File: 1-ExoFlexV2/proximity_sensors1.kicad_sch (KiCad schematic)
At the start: 37 parts, among them J100 Jumper, J95 Jumper, J96 Jumper, J97 Jumper, J98 Jumper, J99 Jumper, U45 Inverter, U46 Inverter, U47 Inverter, U62 AND Gate, U63 AND Gate, U64 AND Gate, U65 AND Gate

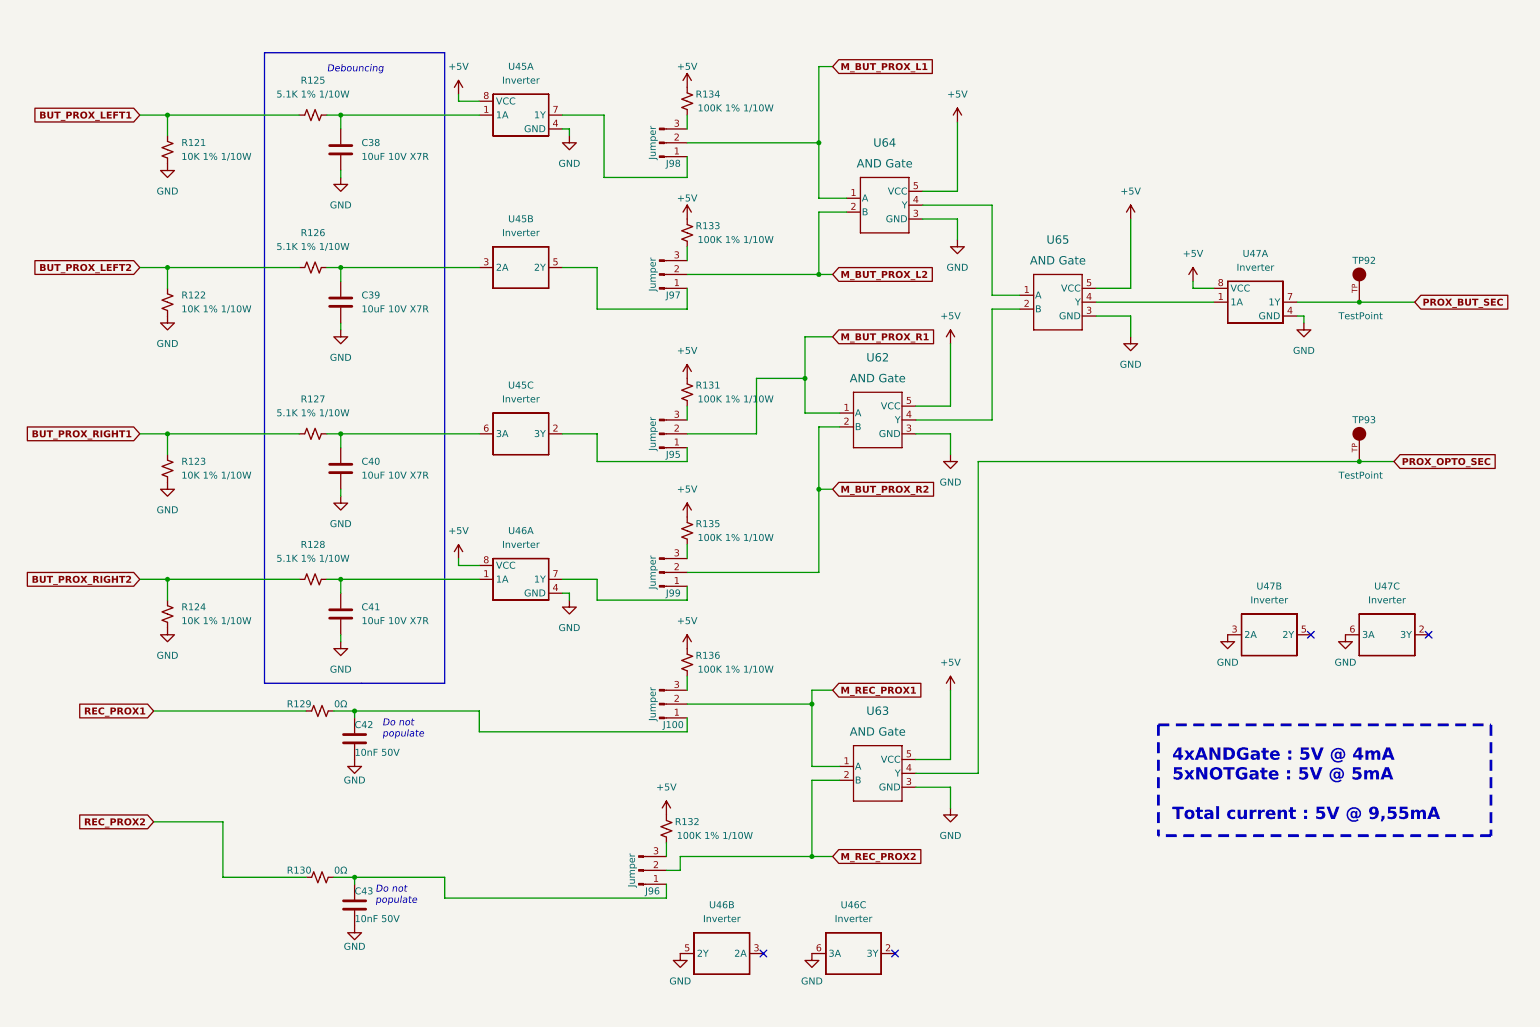
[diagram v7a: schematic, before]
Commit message: Routage pour Review 1
- Replacement des test point pour faciliter le rework
- Correction des erreurs dans le BOM
-
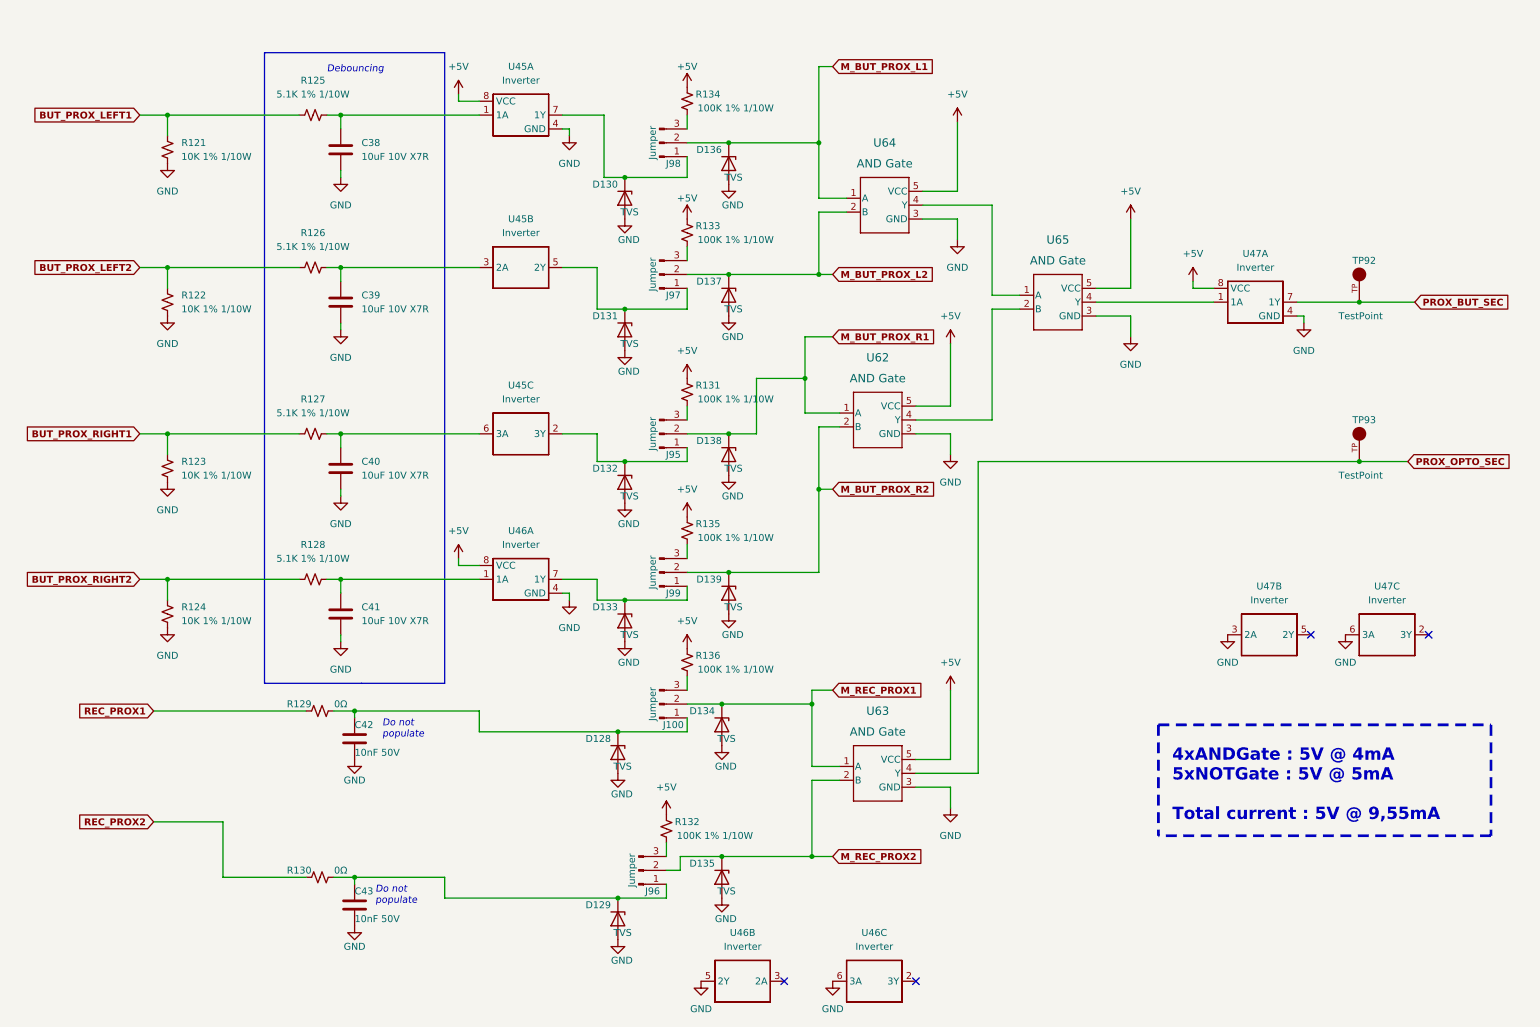
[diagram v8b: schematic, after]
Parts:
- added D128, D129, D130, D131, D132, D133, D134, D135, D136, D137, D138, D139: TVS, FootPrint:DPY2_TEX, symbol Device:D_Zener
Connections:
- net GND: now also D128.2 (A), D129.2 (A), D130.2 (A), D131.2 (A), D132.2 (A), D133.2 (A), D134.2 (A), D135.2 (A), D136.2 (A), D137.2 (A), D138.2 (A), D139.2 (A)
- net M_BUT_PROX_L1: now also D136.1 (K)
- net M_BUT_PROX_L2: now also D137.1 (K)
- net M_BUT_PROX_R1: now also D138.1 (K)
- net M_BUT_PROX_R2: now also D139.1 (K)
- net M_REC_PROX1: now also D134.1 (K)
- net M_REC_PROX2: now also D135.1 (K)
- net at J99.1 (Pin_1), U46.7 (1Y): now also D133.1 (K)
- net at C43.1, J96.1 (Pin_1), R130.2: now also D129.1 (K)
- net at J98.1 (Pin_1), U45.7 (1Y): now also D130.1 (K)
- net at J95.1 (Pin_1), U45.2 (3Y): now also D132.1 (K)
- net at J97.1 (Pin_1), U45.5 (2Y): now also D131.1 (K)
- net at C42.1, J100.1 (Pin_1), R129.2: now also D128.1 (K)
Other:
- moved on the sheet: U46B, U46C
